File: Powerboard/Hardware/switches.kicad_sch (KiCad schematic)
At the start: 15 parts, among them J4 Conn_01x02_Male, J5 RBUS, J6 Conn_01x02_Male, Q1 RSJ250P10TL, Q2 RSJ250P10TL, Q3 RSJ250P10TL, Q4 RSJ250P10TL, U6 LTC4412xS6, U7 LTC4412xS6

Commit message: latest
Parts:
- removed J5: RBUS, Connector_Molex:Molex_Mini-Fit_Jr_5566-06A_2x03_P4.20mm_Vertical, symbol Connector:Conn_01x06_Male
- removed Q1, Q2, Q3, Q4: RSJ250P10TL, Package_TO_SOT_SMD:TO-263-3_TabPin2, symbol iclr:RSJ250P10TL
- added J5: Conn_01x08_Male, Connector_Molex:Molex_Mini-Fit_Jr_5569-08A2_2x04_P4.20mm_Horizontal, symbol Connector:Conn_01x08_Male
- added Q1, Q2, Q3, Q4: PXP012-30QLJ, iclr:PXP01230QLJ, symbol iclr:PXP012-30QLJ
- C23: value C_Polarized_Small -> 1000uF
- C24: value C_Polarized_Small -> 180uF
- J4, J6: footprint Connector_PinHeader_2.54mm:PinHeader_1x02_P2.54mm_Vertical -> Connector_Molex:Molex_Nano-Fit_105313-xx02_1x02_P2.50mm_Horizontal
- JP2, JP3: footprint Jumper:SolderJumper-3_P1.3mm_Bridged2Bar12_RoundedPad1.0x1.5mm -> Jumper:SolderJumper-2_P1.3mm_Bridged_RoundedPad1.0x1.5mm
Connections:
- net +12V: now also Q4.1 (S_1), Q4.2 (S_2), Q4.3 (S_3)
- net 12V_SWITCH: now also JP3.2 (B)
- net CAN+: now also J5.8 (Pin_8)
- net CAN-: now also J5.4 (Pin_4)
- net GND: now also J5.1 (Pin_1), J5.2 (Pin_2), J5.3 (Pin_3)
- net RBUS_uC_V: now reaches U6.1 (VIN)
- net RBUS_uC_V: now also Q2.1 (S_1), Q2.2 (S_2), Q2.3 (S_3)
- net at U6.5 (GATE): now also Q1.4 (G), Q2.4 (G)
- net at C23.1, U6.6 (SENSE): now also J5.5 (Pin_5), Q1.1 (S_1), Q1.2 (S_2), Q1.3 (S_3)
- net at C24.1, U7.6 (SENSE): now also J5.6 (Pin_6), J5.7 (Pin_7), Q3.1 (S_1), Q3.2 (S_2), Q3.3 (S_3)
- net at U7.5 (GATE): now also Q3.4 (G), Q4.4 (G)
- new net: Q3.5 (D_1), Q3.6 (D_2), Q3.7 (D_3), Q3.8 (D_4), Q3.9 (D_5), Q4.5 (D_1), Q4.6 (D_2), Q4.7 (D_3), Q4.8 (D_4), Q4.9 (D_5)
- new net: Q1.5 (D_1), Q1.6 (D_2), Q1.7 (D_3), Q1.8 (D_4), Q1.9 (D_5), Q2.5 (D_1), Q2.6 (D_2), Q2.7 (D_3), Q2.8 (D_4), Q2.9 (D_5)

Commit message: waiting for review
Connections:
- net CAN-: now also J5.7 (Pin_7); no longer J5.4 (Pin_4)
- net at C23.1, Q1.1 (S_1), Q1.2 (S_2)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: now also J5.4 (Pin_4); no longer J5.5 (Pin_5)
- net at C24.1, J5.6 (Pin_6), Q3.1 (S_1)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: now also J5.5 (Pin_5); no longer J5.7 (Pin_7)
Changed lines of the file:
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@@
 (kicad_sch (version 20211123) (generator eeschema)
   (paper "A4")
+  (junction (at 140.462 146.05) (diameter 0) (color 0 0 0 0)
+  )
   (junction (at 155.194 83.82) (diameter 0) (color 0 0 0 0)
   )
@@
   )
   (junction (at 87.122 98.806) (diameter 0) (color 0 0 0 0)
-  )
-  (junction (at 143.002 146.05) (diameter 0) (color 0 0 0 0)
   )
   (junction (at 189.484 115.062) (diameter 0) (color 0 0 0 0)
@@
     (stroke (width 0) (type default) (color 0 0 0 0))
   )
-  (wire (pts (xy 143.002 146.05) (xy 145.542 146.05))
-    (stroke (width 0) (type default) (color 0 0 0 0))
-  )
   (wire (pts (xy 155.194 74.676) (xy 146.558 74.676))
     (stroke (width 0) (type default) (color 0 0 0 0))
@@
     (stroke (width 0) (type default) (color 0 0 0 0))
   )
-  (wire (pts (xy 137.922 146.05) (xy 143.002 146.05))
+  (wire (pts (xy 137.922 146.05) (xy 140.462 146.05))
     (stroke (width 0) (type default) (color 0 0 0 0))
   )
@@
     (stroke (width 0) (type default) (color 0 0 0 0))
   )
-  (wire (pts (xy 140.462 155.448) (xy 140.462 148.336))
-    (stroke (width 0) (type default) (color 0 0 0 0))
-  )
   (wire (pts (xy 130.302 155.448) (xy 123.698 155.448))
     (stroke (width 0) (type default) (color 0 0 0 0))
@@
     (stroke (width 0) (type default) (color 0 0 0 0))
   )
+  (wire (pts (xy 140.462 146.05) (xy 140.462 155.448))
+    (stroke (width 0) (type default) (color 0 0 0 0))
+  )
   (wire (pts (xy 104.902 142.748) (xy 130.302 142.748))
     (stroke (width 0) (type default) (color 0 0 0 0))
@@
     (stroke (width 0) (type default) (color 0 0 0 0))
   )
-  (wire (pts (xy 140.462 148.336) (xy 130.302 148.336))
-    (stroke (width 0) (type default) (color 0 0 0 0))
-  )
   (wire (pts (xy 104.902 84.836) (xy 104.902 92.456))
     (stroke (width 0) (type default) (color 0 0 0 0))
@@
     (stroke (width 0) (type default) (color 0 0 0 0))
   )
+  (wire (pts (xy 140.462 146.05) (xy 143.002 146.05))
+    (stroke (width 0) (type default) (color 0 0 0 0))
+  )
   (wire (pts (xy 140.716 74.676) (xy 140.716 72.644))
     (stroke (width 0) (type default) (color 0 0 0 0))
@@
     (stroke (width 0) (type default) (color 0 0 0 0))
   )
+  (wire (pts (xy 130.302 148.336) (xy 137.922 148.336))
+    (stroke (width 0) (type default) (color 0 0 0 0))
+  )
   (wire (pts (xy 189.484 85.852) (xy 192.024 85.852))
     (stroke (width 0) (type default) (color 0 0 0 0))
@@
     (stroke (width 0) (type default) (color 0 0 0 0))
   )
+  (wire (pts (xy 137.922 148.336) (xy 137.922 155.448))
+    (stroke (width 0) (type default) (color 0 0 0 0))
+  )
   (wire (pts (xy 178.816 60.452) (xy 178.816 85.852))
     (stroke (width 0) (type default) (color 0 0 0 0))
@@
   )
   (wire (pts (xy 70.612 85.09) (xy 70.612 88.646))
-    (stroke (width 0) (type default) (color 0 0 0 0))
-  )
-  (wire (pts (xy 145.542 146.05) (xy 145.542 155.448))
     (stroke (width 0) (type default) (color 0 0 0 0))
   )
@@
     (effects (font (size 1.27 1.27)) (justify left))
   )
-  (hierarchical_label "CAN-" (shape input) (at 137.922 155.448 90)
-    (effects (font (size 1.27 1.27)) (justify left))
-  )
+  (hierarchical_label "CAN-" (shape input) (at 145.542 155.448 90)
+    (effects (font (size 1.27 1.27)) (justify left))
+  )

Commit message: changed nanofits for pin headers, made space for usb casing
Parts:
- J4, J6: footprint Connector_Molex:Molex_Nano-Fit_105313-xx02_1x02_P2.50mm_Horizontal -> Connector_PinHeader_2.54mm:PinHeader_1x02_P2.54mm_Vertical
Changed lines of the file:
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@@
       (effects (font (size 1.27 1.27)) (justify left))
     )
-    (property "Footprint" "Connector_Molex:Molex_Nano-Fit_105313-xx02_1x02_P2.50mm_Horizontal" (id 2) (at 66.548 80.01 0)
+    (property "Footprint" "Connector_PinHeader_2.54mm:PinHeader_1x02_P2.54mm_Vertical" (id 2) (at 66.548 80.01 0)
       (effects (font (size 1.27 1.27)) hide)
     )
@@
       (effects (font (size 1.27 1.27)) (justify left))
     )
-    (property "Footprint" "Connector_Molex:Molex_Nano-Fit_105313-xx02_1x02_P2.50mm_Horizontal" (id 2) (at 151.13 78.74 0)
-      (effects (font (size 1.27 1.27)) hide)
-    )
+    (property "Footprint" "Connector_PinHeader_2.54mm:PinHeader_1x02_P2.54mm_Vertical" (id 2) (at 151.13 78.74 0)
+      (effects (font (size 1.27 1.27)) hide)
+    )

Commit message: i2c breakout, general clean up
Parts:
- J5: footprint Connector_Molex:Molex_Mini-Fit_Jr_5569-08A2_2x04_P4.20mm_Horizontal -> iclr:Molex_Mini-Fit_Jr_5569-08A2_2x04_P4.20mm_Horizontal

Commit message: vias fixed, ready for review
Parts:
- added R24, R26: R_Small, Resistor_SMD:R_0402_1005Metric, symbol Device:R_Small
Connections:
- net GND: now also R26.2
- net at C23.1, J5.4 (Pin_4), Q1.1 (S_1)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: now also R24.1
- new net 3V3LOG: R24.2, R26.1
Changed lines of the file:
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@@
   (junction (at 192.024 60.452) (diameter 0) (color 0 0 0 0)
+  )
+  (junction (at 104.902 142.748) (diameter 0) (color 0 0 0 0)
   )
   (junction (at 186.944 85.852) (diameter 0) (color 0 0 0 0)
@@
     (stroke (width 0) (type default))
   )
+  (wire (pts (xy 104.902 150.876) (xy 104.902 153.162))
+    (stroke (width 0) (type default))
+  )
   (wire (pts (xy 197.104 111.252) (xy 203.454 111.252))
     (stroke (width 0) (type default))
@@
   )
   (wire (pts (xy 104.902 51.816) (xy 104.902 59.436))
+    (stroke (width 0) (type default))
+  )
+  (wire (pts (xy 104.902 142.748) (xy 104.902 145.796))
     (stroke (width 0) (type default))
   )
@@
   )
   (hierarchical_label "3V3_SWITCH" (shape input) (at 70.612 68.072 90) (fields_autoplaced)
+    (effects (font (size 1.27 1.27)) (justify left))
+  )
+  (hierarchical_label "3V3LOG" (shape input) (at 104.902 151.892 0) (fields_autoplaced)
     (effects (font (size 1.27 1.27)) (justify left))
   )
@@
     )
   )
+  (symbol (lib_id "Device:R_Small") (at 104.902 155.702 0) (unit 1)
+    (in_bom yes) (on_board yes) (dnp no) (fields_autoplaced)
+    (property "Reference" "R26" (at 106.4006 155.0583 0)
+      (effects (font (size 1.27 1.27)) (justify left))
+    )
+    (property "Value" "R_Small" (at 106.4006 156.9793 0)
+      (effects (font (size 1.27 1.27)) (justify left))
+    )
+    (property "Footprint" "Resistor_SMD:R_0402_1005Metric" (at 104.902 155.702 0)
+      (effects (font (size 1.27 1.27)) hide)
+    )
+    (property "Datasheet" "~" (at 104.902 155.702 0)
+      (effects (font (size 1.27 1.27)) hide)
+    )
+    (pin "1")
+    (pin "2")
+    (instances
+      (project "Switcher"
+        (path "/e63e39d7-6ac0-4ffd-8aa3-1841a4541b55/133f56f4-a29c-4cbf-87b7-9d99a292e3c0"
+          (reference "R26") (unit 1)
+        )
+      )
+    )
+  )
   (symbol (lib_id "Jumper:SolderJumper_2_Bridged") (at 155.194 70.866 90) (unit 1)
     (in_bom yes) (on_board yes) (dnp no) (fields_autoplaced)
@@
         )
       )
+    )
+  )
+  (symbol (lib_id "power:GND") (at 104.902 158.242 0) (unit 1)
+    (in_bom yes) (on_board yes) (dnp no) (fields_autoplaced)
+    (property "Reference" "#PWR01" (at 104.902 164.592 0)
+      (effects (font (size 1.27 1.27)) hide)
+    )
+    (property "Value" "GND" (at 104.902 162.6854 0)
+      (effects (font (size 1.27 1.27)))
+    )
+    (property "Footprint" "" (at 104.902 158.242 0)
+      (effects (font (size 1.27 1.27)) hide)
+    )
+    (property "Datasheet" "" (at 104.902 158.242 0)
+      (effects (font (size 1.27 1.27)) hide)
+    )
+    (pin "1")
+    (instances
+      (project "Switcher"
+        (path "/e63e39d7-6ac0-4ffd-8aa3-1841a4541b55/133f56f4-a29c-4cbf-87b7-9d99a292e3c0"
+          (reference "#PWR01") (unit 1)
+        )
+      )
+    )
+  )
+  (symbol (lib_id "Device:R_Small") (at 104.902 148.336 0) (unit 1)
+    (in_bom yes) (on_board yes) (dnp no) (fields_autoplaced)
+    (property "Reference" "R24" (at 106.4006 147.6923 0)
+      (effects (font (size 1.27 1.27)) (justify left))
+    )
+    (property "Value" "R_Small" (at 106.4006 149.6133 0)
+      (effects (font (size 1.27 1.27)) (justify left))
+    )
+    (property "Footprint" "Resistor_SMD:R_0402_1005Metric" (at 104.902 148.336 0)
+      (effects (font (size 1.27 1.27)) hide)
+    )
+    (property "Datasheet" "~" (at 104.902 148.336 0)
+      (effects (font (size 1.27 1.27)) hide)
+    )
+    (pin "1")
+    (pin "2")
+    (instances
+      (project "Switcher"
+        (path "/e63e39d7-6ac0-4ffd-8aa3-1841a4541b55/133f56f4-a29c-4cbf-87b7-9d99a292e3c0"
+          (reference "R24") (unit 1)
+        )
+      )

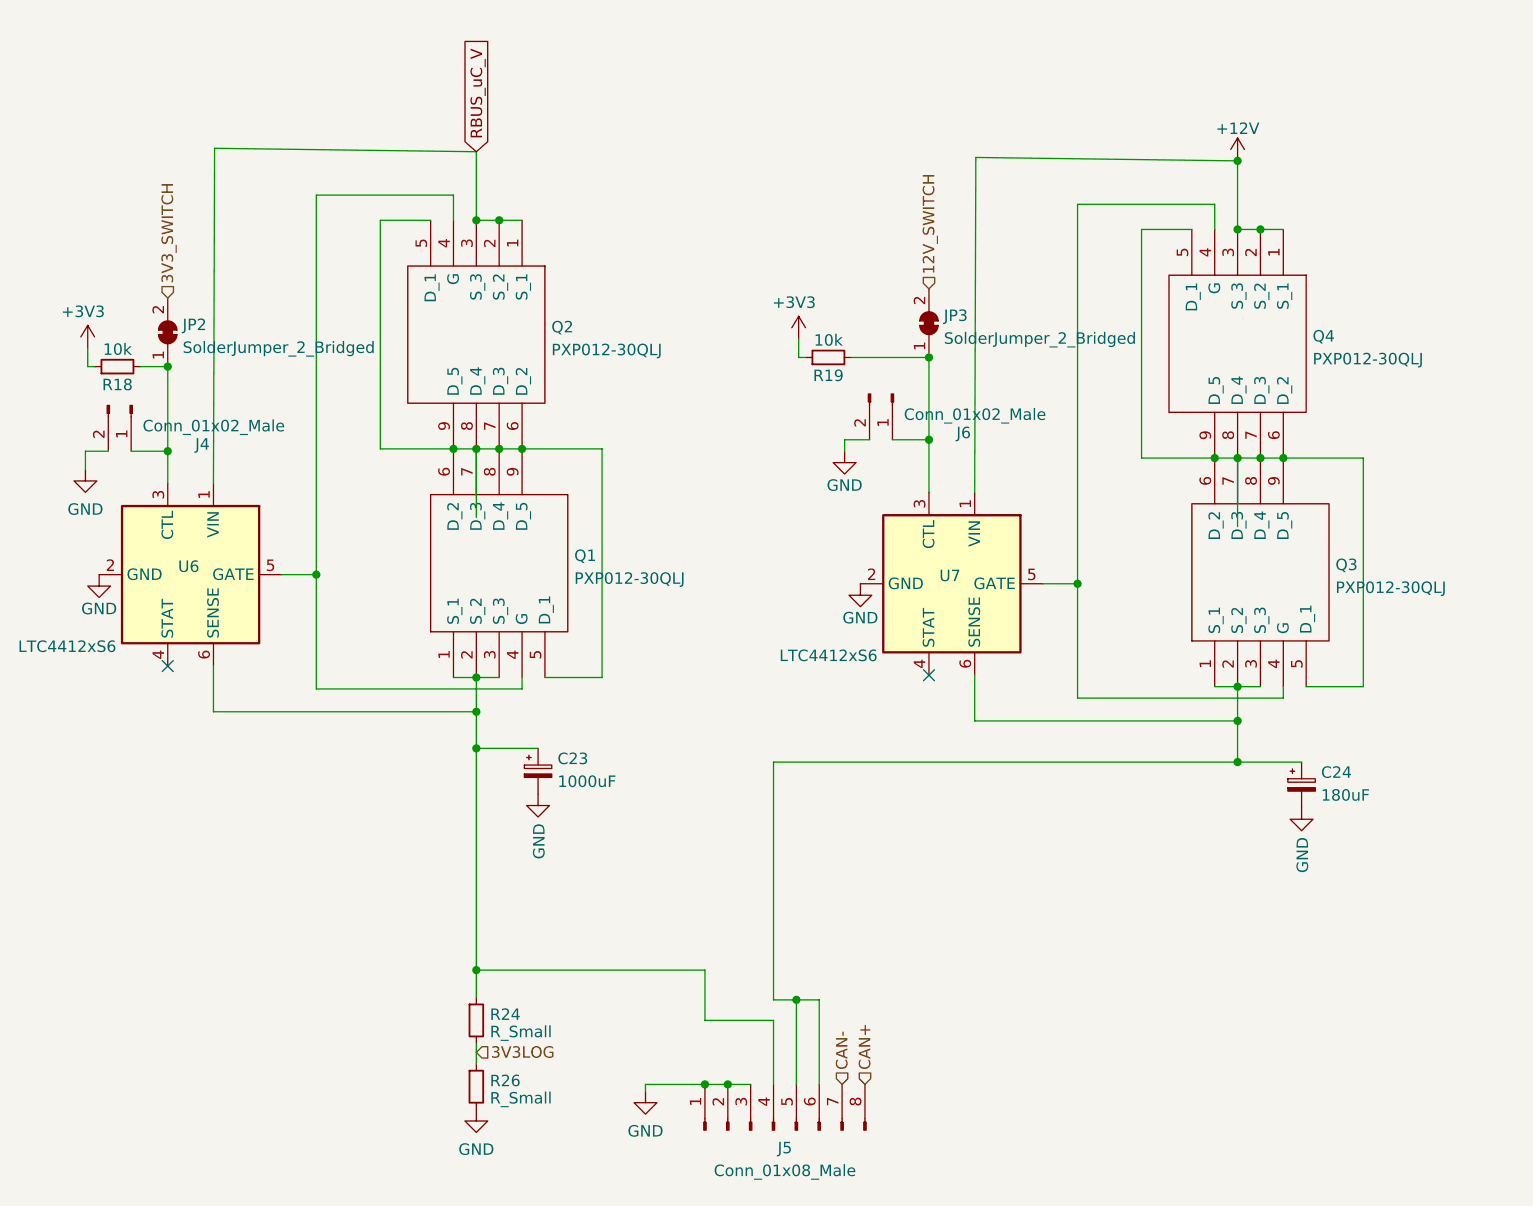
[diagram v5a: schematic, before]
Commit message: mosfet flipping
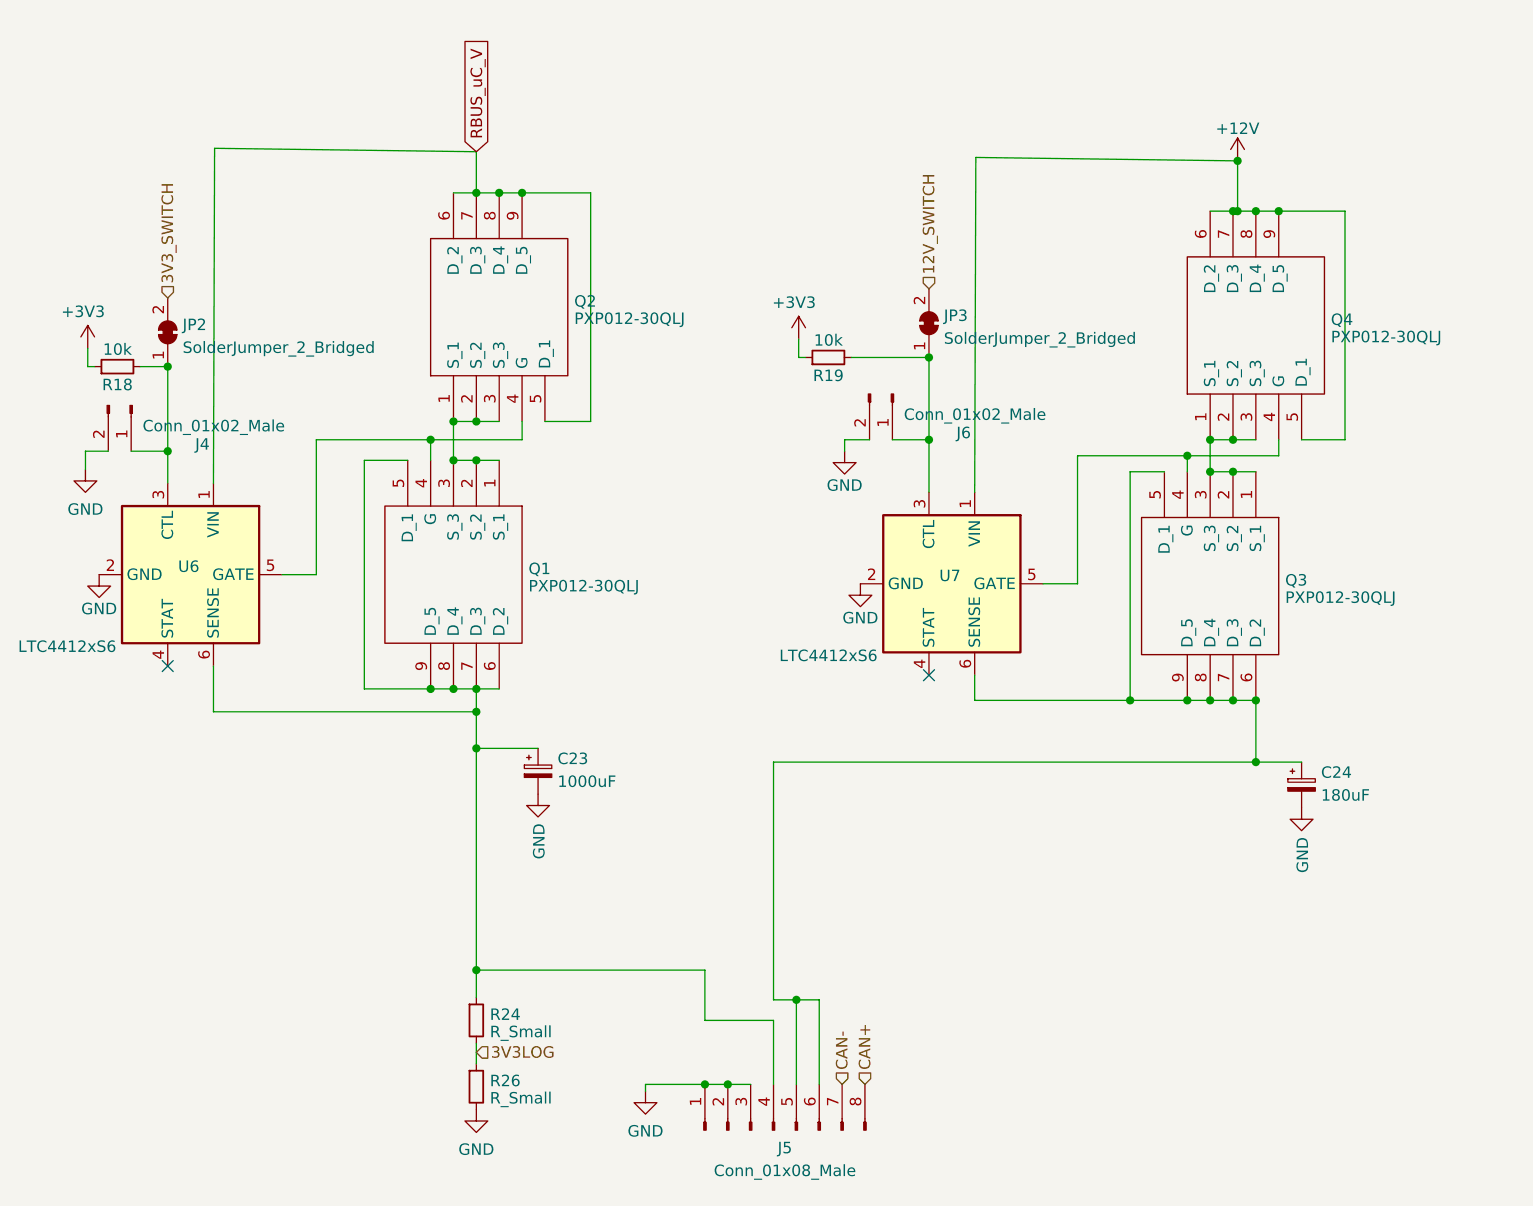
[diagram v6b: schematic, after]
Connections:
- net +12V: now also Q4.5 (D_1), Q4.6 (D_2), Q4.7 (D_3), Q4.8 (D_4), Q4.9 (D_5); no longer Q4.1 (S_1), Q4.2 (S_2), Q4.3 (S_3)
- net RBUS_uC_V: now also Q2.5 (D_1), Q2.6 (D_2), Q2.7 (D_3), Q2.8 (D_4), Q2.9 (D_5); no longer Q2.1 (S_1), Q2.2 (S_2), Q2.3 (S_3)
- net at C23.1, J5.4 (Pin_4), R24.1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: now also Q1.5 (D_1), Q1.6 (D_2), Q1.7 (D_3), Q1.8 (D_4), Q1.9 (D_5); no longer Q1.1 (S_1), Q1.2 (S_2), Q1.3 (S_3)
- net at C24.1, J5.5 (Pin_5), J5.6 (Pin_6)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: now also Q3.5 (D_1), Q3.6 (D_2), Q3.7 (D_3), Q3.8 (D_4), Q3.9 (D_5); no longer Q3.1 (S_1), Q3.2 (S_2), Q3.3 (S_3)
- new net: Q3.1 (S_1), Q3.2 (S_2), Q3.3 (S_3), Q4.1 (S_1), Q4.2 (S_2), Q4.3 (S_3)
- new net: Q1.1 (S_1), Q1.2 (S_2), Q1.3 (S_3), Q2.1 (S_1), Q2.2 (S_2), Q2.3 (S_3)
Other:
- moved on the sheet: Q1, Q2, Q3, Q4
